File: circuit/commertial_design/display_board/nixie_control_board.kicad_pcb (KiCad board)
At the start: 2 copper layers, 200 x 63 mm, 22 parts, among them P1 CONN_02X03, P5 CONN_01X08, P6 CONN_01X12, SW1 SW_PUSH, SW2 SW_PUSH, SW3 SW_PUSH, U10 IN-14, U11 IN-14, U12 IN-14, U13 IN-14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

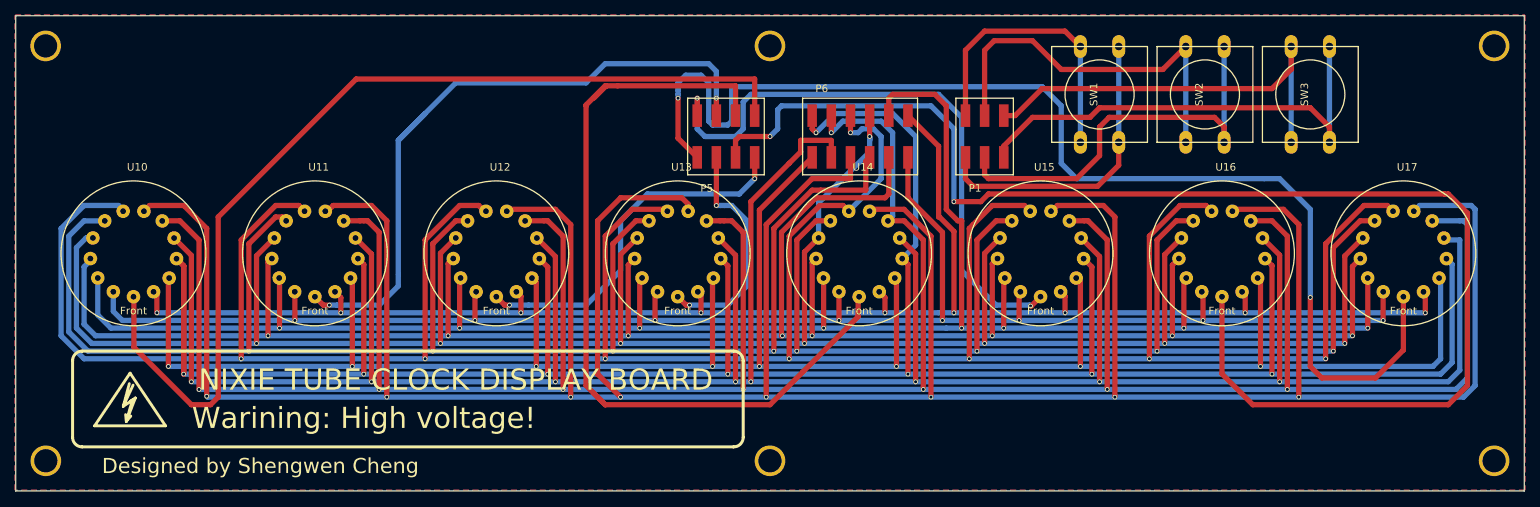
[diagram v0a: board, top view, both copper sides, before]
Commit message: Layout need to be arranged, scheme is finished
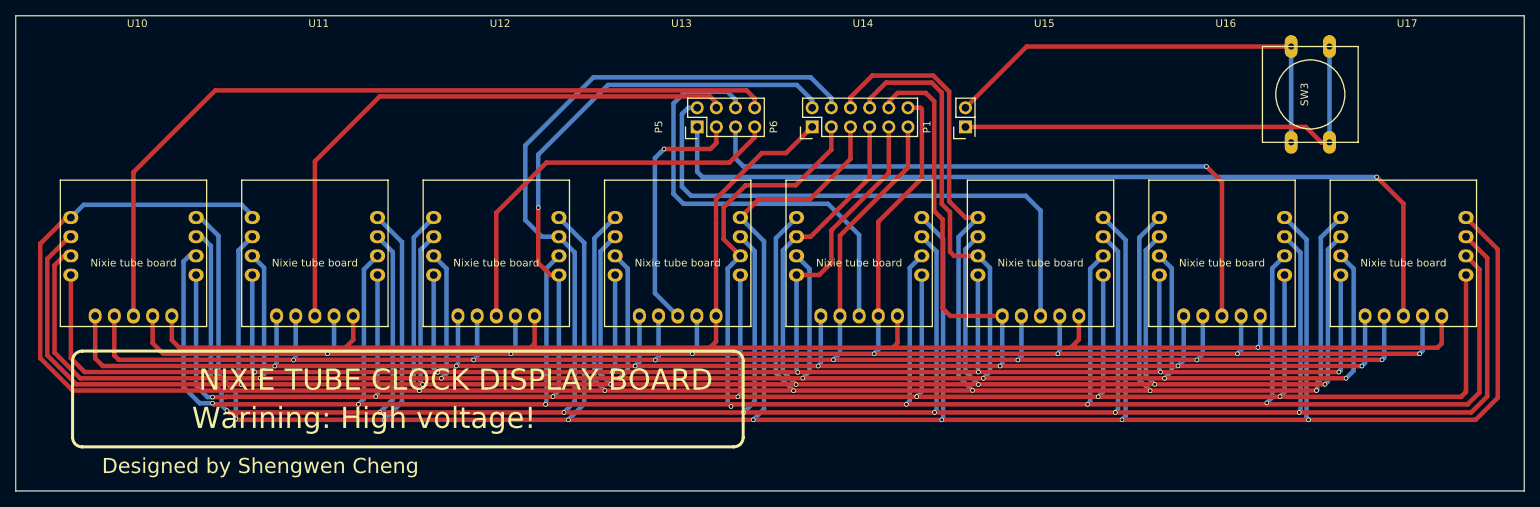
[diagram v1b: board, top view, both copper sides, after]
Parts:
- removed REF** (x2): Symbol_HighVoltage_Type2_CopperTop_VerySmall, warning:warning
- removed REF** (x6): MountingHole_2.2mm_M2, Mounting_Holes:MountingHole_2.2mm_M2
- removed SW1, SW2: SW_PUSH, button:SW_PUSH-12mm
- P1: value CONN_02X03 -> CONN_02X01; footprint SMD_PIN_2_BY_3:SMD_PIN_2_BY_3 -> Pin_Headers:Pin_Header_Straight_2x01
- P5: footprint SMD_PIN_2_BY_4:SMD_PIN_2_BY_4 -> Pin_Headers:Pin_Header_Straight_2x04
- P6: footprint SMD_PIN_2_BY_6:SMD_PIN_2_BY_6 -> Pin_Headers:Pin_Header_Straight_2x06
- SW3: footprint button:SW_PUSH-12mm -> Buttons_Switches_ThroughHole:SW_PUSH-12mm
- U10, U11, U12, U13, U14, U15, U16, U17: footprint IN-14:IN-14 -> IN-14-board:IN-14
- turned P1 to 90 degrees
- turned P5 to 90 degrees
- turned P6 to 90 degrees
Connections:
- SW3 pad 1: Net-(P1-Pad6) -> Net-(P1-Pad2)
- SW3 pad 2: Net-(P1-Pad5) -> Net-(P1-Pad1)
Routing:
- net anode4: track 183.5 -> 87.7 mm, vias 2 -> 1
- net Net-(P1-Pad5): track 62.6 -> 0.00 mm
- net cathode0: track 294.4 -> 235.2 mm, vias 8 -> 1
- net cathode6: track 473.9 -> 416.8 mm
- net Net-(P1-Pad6): track 56.4 -> 0.00 mm
- net Net-(P1-Pad3): track 56.2 -> 0.00 mm
- net anode3: track 112.0 -> 59.9 mm
- net Net-(P1-Pad4): track 51.4 -> 0.00 mm
- net anode8: track 159.3 -> 116.2 mm, vias 2 -> 1
- net cathode3: track 306.9 -> 345.9 mm, vias 8 -> 7
- net cathode7: track 399.5 -> 424.6 mm, vias 8 -> 7
- net cathode_comma_left: track 222.5 -> 245.1 mm, vias 8 -> 7
- net Net-(P1-Pad1): track 40.5 -> 61.8 mm
- net anode1: track 128.9 -> 107.6 mm
- net Net-(P1-Pad2): track 38.5 -> 59.2 mm
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- removed copper zone on B.Cu, net (none)
- removed copper zone on F.Cu, net (none)

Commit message: Update commertial board
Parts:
- added REF**: 1pin, Connect:1pin, F.Cu at (248.1, 74.6)
- added REF**: 1pin, Connect:1pin, F.Cu at (248.1, 129.6)
- added REF**: 1pin, Connect:1pin, F.Cu at (56.1, 74.6)
- added REF**: 1pin, Connect:1pin, F.Cu at (56.1, 129.6)
- added REF**: Symbol_HighVoltage_Type2_CopperTop_VerySmall, warning:warning, F.Cu at (67.5, 122.1)
- added REF**: Symbol_HighVoltage_Type2_CopperTop_VerySmall, warning:warning, B.Cu at (67.5, 81.5)
- moved U14 0.21 mm to (164.1, 102.1)
- moved U15 0.21 mm to (188.1, 102.1)
- moved U17 0.21 mm to (236.2, 102.1)
- moved U10 0.20 mm to (67.9, 102.1)
- moved U11 0.20 mm to (91.9, 102.1)
- moved U12 0.20 mm to (116.0, 102.1)
- moved U13 0.20 mm to (140.0, 102.1)
- moved U16 0.20 mm to (212.2, 102.1)
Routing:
- net cathode8: track 362.6 -> 368.1 mm
- net cathode3: track 345.9 -> 347.7 mm
- net cathode9: track 357.3 -> 358.0 mm

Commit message: Fix PCB board
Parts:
- e REF**: renamed from REF**
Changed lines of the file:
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@@
     (visible_elements FFFFFF7F)
     (pcbplotparams
-      (layerselection 0x01030_80000001)
+      (layerselection 0x010f0_80000001)
       (usegerberextensions true)
       (excludeedgelayer true)
@@
       (drillshape 0)
       (scaleselection 1)
-      (outputdirectory 2016_9_13_DISPLAY_BRD/))
+      (outputdirectory DISPLAY_BRD_VER3/))
   )
   (net 0 "")
@@
   (module Buttons_Switches_ThroughHole:SW_PUSH-12mm (layer F.Cu)
     (at 223.70288 81 90)
-    (fp_text reference SW3 (at 0 -0.762 90) (layer F.SilkS)
+    (fp_text reference SW3 (at -0.49844 0 180) (layer F.SilkS)
       (effects (font (size 1 1) (thickness 0.15)))
     )
@@
   (module IN-14-board:IN-14 (layer F.Cu)
     (at 164.095 102.06844)
-    (fp_text reference U14 (at 0.5 -30.48) (layer F.SilkS)
-      (effects (font (size 1 1) (thickness 0.15)))
-    )
-    (fp_text value IN-14 (at 0 -27.17) (layer F.Fab)
+    (fp_text reference U14 (at -0.08212 -1.52) (layer F.SilkS)
+      (effects (font (size 1 1) (thickness 0.15)))
+    )
+    (fp_text value IN-14 (at -0.08212 -0.25) (layer F.Fab)
       (effects (font (size 1 1) (thickness 0.15)))
     )
@@
   (module IN-14-board:IN-14 (layer F.Cu)
     (at 188.145 102.06844)
-    (fp_text reference U15 (at 0.5 -30.48) (layer F.SilkS)
-      (effects (font (size 1 1) (thickness 0.15)))
-    )
-    (fp_text value IN-14 (at 0 -27.17) (layer F.Fab)
+    (fp_text reference U15 (at -0.00212 -1.52) (layer F.SilkS)
+      (effects (font (size 1 1) (thickness 0.15)))
+    )
+    (fp_text value IN-14 (at -0.00212 -0.25) (layer F.Fab)
       (effects (font (size 1 1) (thickness 0.15)))
     )
@@
   (module IN-14-board:IN-14 (layer F.Cu)
     (at 212.195 102.06844)
-    (fp_text reference U16 (at 0.5 -30.48) (layer F.SilkS)
-      (effects (font (size 1 1) (thickness 0.15)))
-    )
-    (fp_text value IN-14 (at 0 -27.17) (layer F.Fab)
+    (fp_text reference U16 (at 0.07788 -1.52) (layer F.SilkS)
+      (effects (font (size 1 1) (thickness 0.15)))
+    )
+    (fp_text value IN-14 (at 0.07788 -0.25) (layer F.Fab)
       (effects (font (size 1 1) (thickness 0.15)))
     )
@@
   (module IN-14-board:IN-14 (layer F.Cu)
     (at 236.245 102.06844)
-    (fp_text reference U17 (at 0.5 -30.48) (layer F.SilkS)
-      (effects (font (size 1 1) (thickness 0.15)))
-    )
-    (fp_text value IN-14 (at 0 -27.17) (layer F.Fab)
+    (fp_text reference U17 (at 0.15788 -1.52) (layer F.SilkS)
+      (effects (font (size 1 1) (thickness 0.15)))
+    )
+    (fp_text value IN-14 (at 0.15788 -0.25) (layer F.Fab)
       (effects (font (size 1 1) (thickness 0.15)))
     )
@@
   (module IN-14-board:IN-14 (layer F.Cu)
     (at 140.045 102.06844)
-    (fp_text reference U13 (at 0.5 -30.48) (layer F.SilkS)
-      (effects (font (size 1 1) (thickness 0.15)))
-    )
-    (fp_text value IN-14 (at 0 -27.17) (layer F.Fab)
+    (fp_text reference U13 (at -0.16212 -1.52) (layer F.SilkS)
+      (effects (font (size 1 1) (thickness 0.15)))
+    )
+    (fp_text value IN-14 (at -0.16212 -0.25) (layer F.Fab)
       (effects (font (size 1 1) (thickness 0.15)))
     )
@@
   (module IN-14-board:IN-14 (layer F.Cu)
     (at 115.995 102.06844)
-    (fp_text reference U12 (at 0.5 -30.48) (layer F.SilkS)
-      (effects (font (size 1 1) (thickness 0.15)))
-    )
-    (fp_text value IN-14 (at 0 -27.17) (layer F.Fab)
+    (fp_text reference U12 (at -0.24212 -1.52) (layer F.SilkS)
+      (effects (font (size 1 1) (thickness 0.15)))
+    )
+    (fp_text value IN-14 (at -0.24212 -0.25) (layer F.Fab)
       (effects (font (size 1 1) (thickness 0.15)))
     )
@@
   (module IN-14-board:IN-14 (layer F.Cu)
     (at 91.945 102.06844)
-    (fp_text reference U11 (at 0.5 -30.48) (layer F.SilkS)
-      (effects (font (size 1 1) (thickness 0.15)))
-    )
-    (fp_text value IN-14 (at 0 -27.17) (layer F.Fab)
+    (fp_text reference U11 (at -0.32212 -1.52) (layer F.SilkS)
+      (effects (font (size 1 1) (thickness 0.15)))
+    )
+    (fp_text value IN-14 (at -0.32212 -0.25) (layer F.Fab)
       (effects (font (size 1 1) (thickness 0.15)))
     )
@@
   (module IN-14-board:IN-14 (layer F.Cu)
     (at 67.895 102.06844)
-    (fp_text reference U10 (at 0.5 -30.48) (layer F.SilkS)
-      (effects (font (size 1 1) (thickness 0.15)))
-    )
-    (fp_text value IN-14 (at 0 -27.17) (layer F.Fab)
+    (fp_text reference U10 (at -0.40212 -1.52) (layer F.SilkS)
+      (effects (font (size 1 1) (thickness 0.15)))
+    )
+    (fp_text value IN-14 (at -0.40212 -0.25) (layer F.Fab)
       (effects (font (size 1 1) (thickness 0.15)))
     )
@@
     (descr "Through hole pin header")
     (tags "pin header")
-    (fp_text reference P5 (at 0 -5.1 90) (layer F.SilkS)
+    (fp_text reference P5 (at 5.08 0 180) (layer F.SilkS)
       (effects (font (size 1 1) (thickness 0.15)))
     )
@@
     (descr "Through hole pin header")
     (tags "pin header")
-    (fp_text reference P6 (at 0 -5.1 90) (layer F.SilkS)
+    (fp_text reference P6 (at 5.08 0 180) (layer F.SilkS)
       (effects (font (size 1 1) (thickness 0.15)))
     )
@@
     (descr "Through hole pin header")
     (tags "pin header")
-    (fp_text reference P1 (at 0 -5.1 90) (layer F.SilkS)
+    (fp_text reference P1 (at 5.08 0 180) (layer F.SilkS)
       (effects (font (size 1 1) (thickness 0.15)))
     )
@@
     (descr "module 1 pin (ou trou mecanique de percage)")
     (tags DEV)
-    (fp_text reference REF** (at 0 -3.048) (layer F.SilkS)
+    (fp_text reference "e REF**" (at 0 -3.048) (layer F.SilkS) hide
       (effects (font (size 1 1) (thickness 0.15)))
     )
@@
     (descr "module 1 pin (ou trou mecanique de percage)")
     (tags DEV)
-    (fp_text reference REF** (at 0 -3.048) (layer F.SilkS)
+    (fp_text reference REF** (at 0 -3.048) (layer F.SilkS) hide
       (effects (font (size 1 1) (thickness 0.15)))
     )
@@
     (descr "module 1 pin (ou trou mecanique de percage)")
     (tags DEV)
-    (fp_text reference REF** (at 0 -3.048) (layer F.SilkS)
+    (fp_text reference REF** (at 0 -3.048) (layer F.SilkS) hide
       (effects (font (size 1 1) (thickness 0.15)))
     )
@@
     (descr "module 1 pin (ou trou mecanique de percage)")
     (tags DEV)
-    (fp_text reference REF** (at 0 -3.048) (layer F.SilkS)
+    (fp_text reference REF** (at 0 -3.048) (layer F.SilkS) hide
       (effects (font (size 1 1) (thickness 0.15)))
     )
@@
     (descr "Symbol, High Voltage, Type 2, Copper Top, Very Small,")
     (tags "Symbol, High Voltage, Type 2, Copper Top, Very Small,")
-    (fp_text reference REF** (at -11.43 3.81) (layer F.SilkS)
-      (effects (font (size 1 1) (thickness 0.15)))
-    )
+    (fp_text reference REF** (at -11.43 3.81) (layer F.SilkS) hide
+      (effects (font (size 1 1) (thickness 0.15)))
+    )

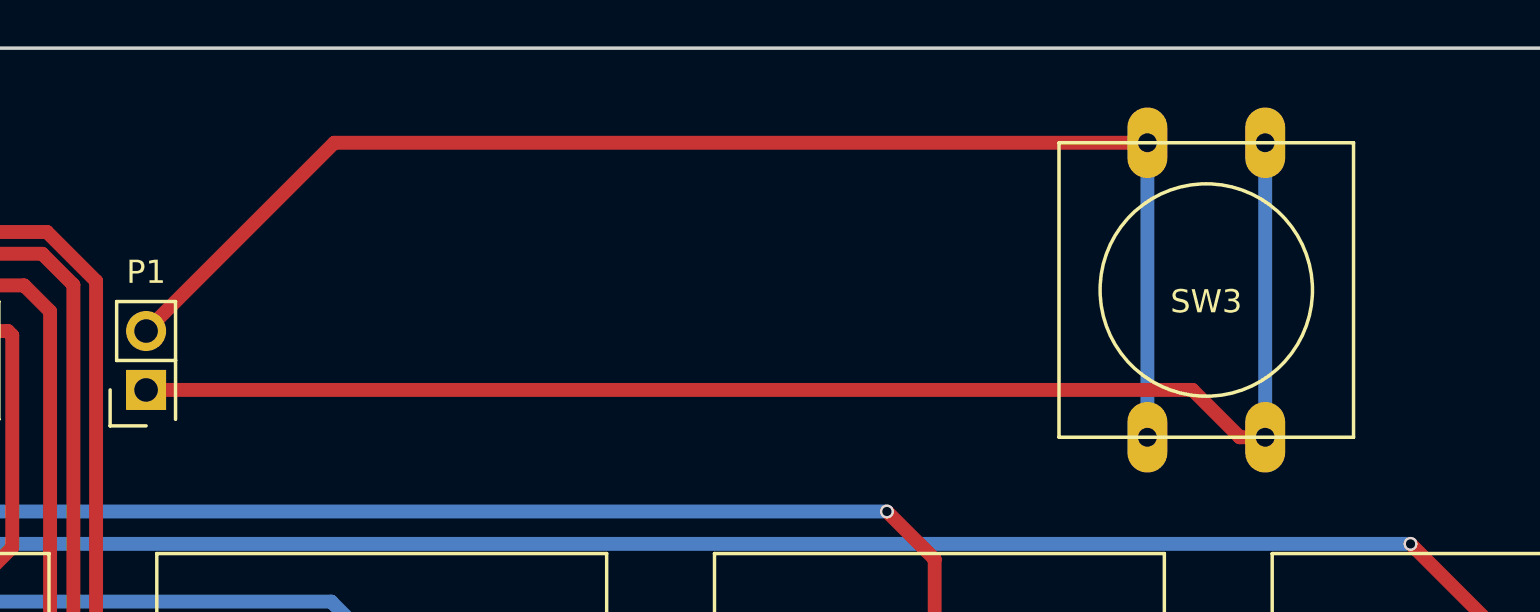
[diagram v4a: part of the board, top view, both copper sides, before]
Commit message: Fix display board button
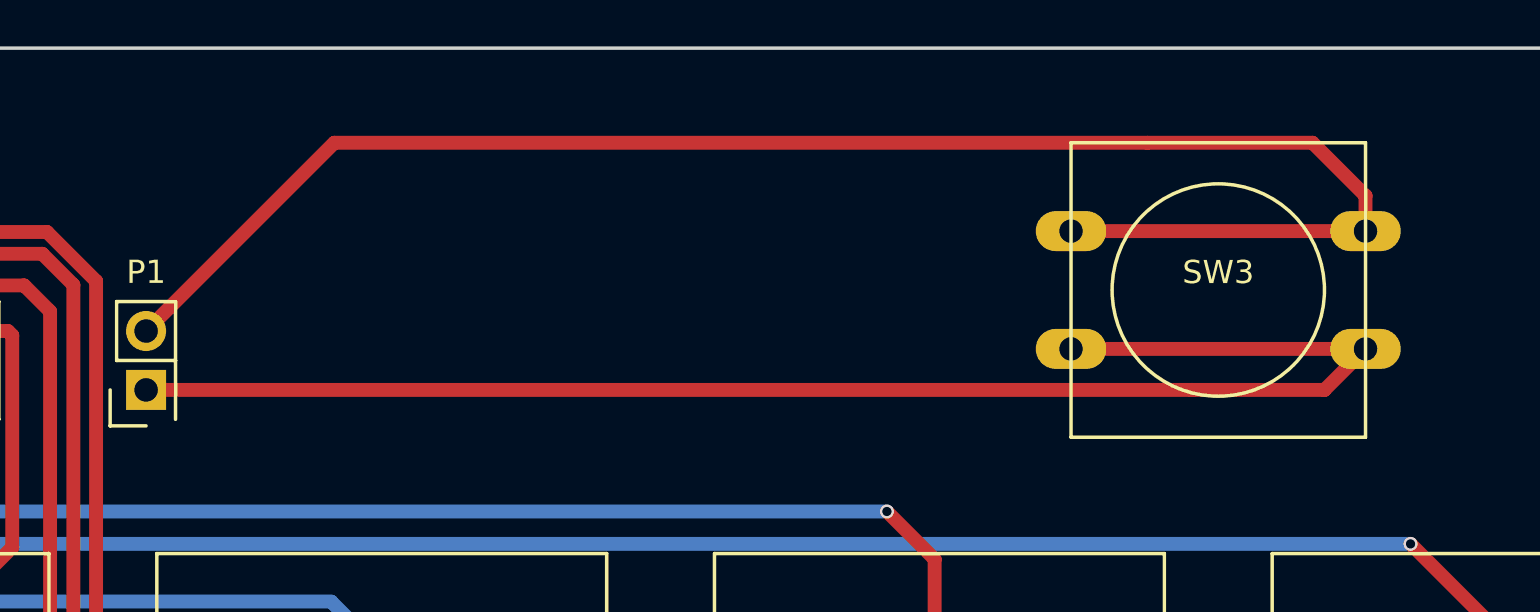
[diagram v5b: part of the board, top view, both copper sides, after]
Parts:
- SW3: footprint Buttons_Switches_ThroughHole:SW_PUSH-12mm -> button:SW_PUSH-12mm
- moved SW3 0.52 mm to (224.2, 81.0), turned to 0 degrees
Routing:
- net Net-(P1-Pad2): track 59.2 -> 71.1 mm
- net Net-(P1-Pad1): track 61.8 -> 66.1 mm
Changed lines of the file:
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@@
-(kicad_pcb (version 4) (host pcbnew 4.0.4+e1-6308~48~ubuntu16.04.1-stable)
+(kicad_pcb (version 4) (host pcbnew 4.0.5-e0-6337~49~ubuntu16.04.1)
   (general
     (links 108)
     (no_connects 0)
-    (area 51.523353 70.493439 252.145001 133.643441)
+    (area 51.994999 70.493439 252.145001 133.643441)
     (thickness 1.6)
     (drawings 26)
-    (tracks 629)
+    (tracks 633)
     (zones 0)
     (modules 18)
@@
   )
   (setup
-    (last_trace_width 0.25)
+    (last_trace_width 0.6)
     (user_trace_width 0.55)
     (user_trace_width 0.6)
@@
     (add_net cathode_comma_right)
   )
-  (module Buttons_Switches_ThroughHole:SW_PUSH-12mm (layer F.Cu)
-    (at 223.70288 81 90)
-    (fp_text reference SW3 (at -0.49844 0 180) (layer F.SilkS)
-      (effects (font (size 1 1) (thickness 0.15)))
-    )
-    (fp_text value SW_PUSH (at 0 1.016 90) (layer F.Fab)
-      (effects (font (size 1 1) (thickness 0.15)))
-    )
-    (fp_circle (center 0 0) (end 3.81 2.54) (layer F.SilkS) (width 0.15))
-    (fp_line (start -6.35 -6.35) (end 6.35 -6.35) (layer F.SilkS) (width 0.15))
-    (fp_line (start 6.35 -6.35) (end 6.35 6.35) (layer F.SilkS) (width 0.15))
-    (fp_line (start 6.35 6.35) (end -6.35 6.35) (layer F.SilkS) (width 0.15))
-    (fp_line (start -6.35 6.35) (end -6.35 -6.35) (layer F.SilkS) (width 0.15))
-    (pad 1 thru_hole oval (at 6.35 -2.54 90) (size 3.048 1.7272) (drill 0.8128) (layers *.Cu *.Mask F.SilkS)
-      (net 21 "Net-(P1-Pad2)"))
-    (pad 2 thru_hole oval (at 6.35 2.54 90) (size 3.048 1.7272) (drill 0.8128) (layers *.Cu *.Mask F.SilkS)
-      (net 20 "Net-(P1-Pad1)"))
-    (pad 1 thru_hole oval (at -6.35 -2.54 90) (size 3.048 1.7272) (drill 0.8128) (layers *.Cu *.Mask F.SilkS)
-      (net 21 "Net-(P1-Pad2)"))
-    (pad 2 thru_hole oval (at -6.35 2.54 90) (size 3.048 1.7272) (drill 0.8128) (layers *.Cu *.Mask F.SilkS)
-      (net 20 "Net-(P1-Pad1)"))
-    (model Buttons_Switches_ThroughHole.3dshapes/SW_PUSH-12mm.wrl
-      (at (xyz 0 0 0))
-      (scale (xyz 4 4 4))
-      (rotate (xyz 0 0 0))
-    )
-  )
   (module IN-14-board:IN-14 (layer F.Cu)
     (at 164.095 102.06844)
@@
     (fp_line (start 4.699 -2.794) (end -4.699 -2.794) (layer B.SilkS) (width 0.381))
     (fp_line (start -4.699 -2.794) (end 0 4.191) (layer B.SilkS) (width 0.381))
+  )
+  (module button:SW_PUSH-12mm (layer F.Cu)
+    (at 224.22 81)
+    (fp_text reference SW3 (at 0 -0.762) (layer F.SilkS)
+      (effects (font (size 1 1) (thickness 0.15)))
+    )
+    (fp_text value SW_PUSH (at 0 1.016) (layer F.Fab)
+      (effects (font (size 1 1) (thickness 0.15)))
+    )
+    (fp_circle (center 0 0) (end 3.81 2.54) (layer F.SilkS) (width 0.15))
+    (fp_line (start -6.35 -6.35) (end 6.35 -6.35) (layer F.SilkS) (width 0.15))
+    (fp_line (start 6.35 -6.35) (end 6.35 6.35) (layer F.SilkS) (width 0.15))
+    (fp_line (start 6.35 6.35) (end -6.35 6.35) (layer F.SilkS) (width 0.15))
+    (fp_line (start -6.35 6.35) (end -6.35 -6.35) (layer F.SilkS) (width 0.15))
+    (pad 1 thru_hole oval (at 6.35 -2.54) (size 3.048 1.7272) (drill 1.01) (layers *.Cu *.Mask F.SilkS)
+      (net 21 "Net-(P1-Pad2)"))
+    (pad 2 thru_hole oval (at 6.35 2.54) (size 3.048 1.7272) (drill 1.01) (layers *.Cu *.Mask F.SilkS)
+      (net 20 "Net-(P1-Pad1)"))
+    (pad 1 thru_hole oval (at -6.35 -2.54) (size 3.048 1.7272) (drill 1.01) (layers *.Cu *.Mask F.SilkS)
+      (net 21 "Net-(P1-Pad2)"))
+    (pad 2 thru_hole oval (at -6.35 2.54) (size 3.048 1.7272) (drill 1.01) (layers *.Cu *.Mask F.SilkS)
+      (net 20 "Net-(P1-Pad1)"))
+    (model Buttons_Switches_ThroughHole.3dshapes/SW_PUSH-12mm.wrl
+      (at (xyz 0 0 0))
+      (scale (xyz 4 4 4))
+      (rotate (xyz 0 0 0))
+    )
   )
   (gr_text "Designed by Shengwen Cheng" (at 85.01888 73.87844 180) (layer B.SilkS)
@@
   (via (at 232.5116 91.948) (size 0.6) (drill 0.4) (layers F.Cu B.Cu) (net 19))
   (segment (start 232.5116 91.948) (end 236.04 95.4764) (width 0.6) (layer F.Cu) (net 19))
-  (segment (start 226.24288 87.35) (end 225.15008 87.35) (width 0.6) (layer F.Cu) (net 20))
-  (segment (start 223.10852 85.30844) (end 177.98288 85.30844) (width 0.6) (layer F.Cu) (net 20))
-  (segment (start 225.15008 87.35) (end 223.10852 85.30844) (width 0.6) (layer F.Cu) (net 20))
-  (segment (start 226.24288 74.65) (end 226.24288 87.35) (width 0.6) (layer B.Cu) (net 20))
+  (segment (start 217.87 83.54) (end 230.57 83.54) (width 0.6) (layer F.Cu) (net 20) (status C00000))
+  (segment (start 223.06788 85.30844) (end 228.80156 85.30844) (width 0.6) (layer F.Cu) (net 20))
+  (segment (start 228.80156 85.30844) (end 230.57 83.54) (width 0.6) (layer F.Cu) (net 20) (status 800000))
+  (segment (start 223.10852 85.30844) (end 223.06788 85.30844) (width 0.6) (layer F.Cu) (net 20))
+  (segment (start 223.06788 85.30844) (end 177.98288 85.30844) (width 0.6) (layer F.Cu) (net 20))
+  (segment (start 217.87 78.46) (end 230.57 78.46) (width 0.6) (layer F.Cu) (net 21) (status C00000))
+  (segment (start 221.16288 74.65) (end 228.28444 74.65) (width 0.6) (layer F.Cu) (net 21))
+  (segment (start 177.98288 82.76844) (end 186.10132 74.65) (width 0.6) (layer F.Cu) (net 21))
   (segment (start 221.16288 74.65) (end 186.10132 74.65) (width 0.6) (layer F.Cu) (net 21))
-  (segment (start 186.10132 74.65) (end 177.98288 82.76844) (width 0.6) (layer F.Cu) (net 21))
-  (segment (start 221.16288 74.65) (end 221.16288 87.35) (width 0.6) (layer B.Cu) (net 21))
+  (segment (start 230.57 76.93556) (end 230.57 78.46) (width 0.6) (layer F.Cu) (net 21) (status 800000))
+  (segment (start 228.28444 74.65) (end 230.57 76.93556) (width 0.6) (layer F.Cu) (net 21))
   (segment (start 185.4 115.742498) (end 185.4 110.36844) (width 0.6) (layer B.Cu) (net 22))
   (segment (start 184.9374 116.205098) (end 185.4 115.742498) (width 0.6) (layer B.Cu) (net 22))
